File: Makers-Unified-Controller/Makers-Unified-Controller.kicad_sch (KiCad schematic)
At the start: 52 parts

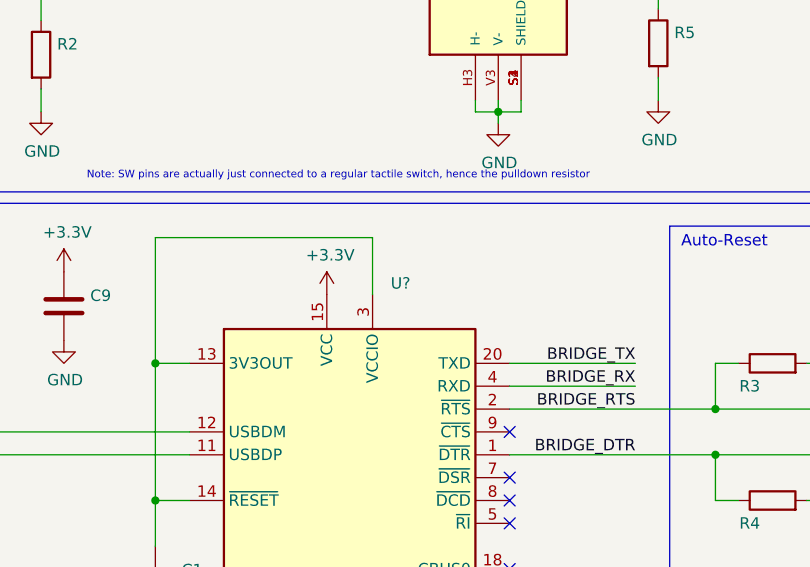
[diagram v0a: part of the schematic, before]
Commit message: Started PCB - removed unused components from revision 1
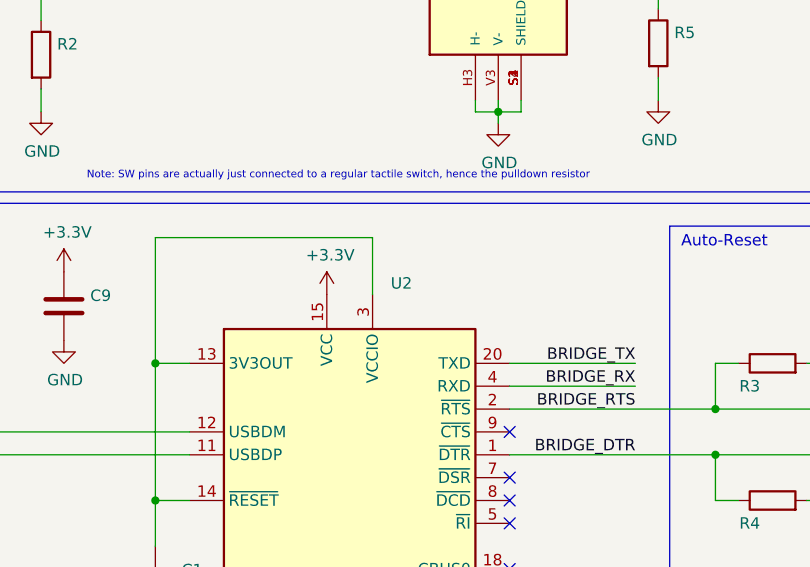
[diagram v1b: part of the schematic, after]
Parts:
- gave numbers to parts that had none: 1

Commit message: fixed BOM item in schematic
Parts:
- U2: digikey_part_number 768-1129-2-ND -> 768-1129-1-ND
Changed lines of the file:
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@@
       (effects (font (size 1.27 1.27)) hide)
     )
-    (property "digikey_part_number" "768-1129-2-ND" (id 4) (at 88.9 144.78 0)
+    (property "digikey_part_number" "768-1129-1-ND" (id 4) (at 88.9 144.78 0)
       (effects (font (size 1.27 1.27)) hide)
     )
@@
     )
     (path "/63021d15-d11b-49d2-bf84-ec09f8b47294/c1425608-5e6d-47c6-a403-895cf960b962"
-      (reference "BT1") (unit 1) (value "PRT-18286") (footprint "Footprint_Imports:PRT18286")
+      (reference "BT1") (unit 1) (value "PRT-18286") (footprint "")
     )
     (path "/00000000-0000-0000-0000-000061acf723"
@@
     )
     (path "/63021d15-d11b-49d2-bf84-ec09f8b47294/048c9335-6615-4fe1-b210-c5621bed4995"
-      (reference "C2") (unit 1) (value "10u") (footprint "Capacitor_SMD:C_0805_2012Metric_Pad1.18x1.45mm_HandSolder")
+      (reference "C2") (unit 1) (value "10u") (footprint "")
     )
     (path "/63021d15-d11b-49d2-bf84-ec09f8b47294/a84c97dc-224b-4aee-818b-6b0092e5b819"
-      (reference "C3") (unit 1) (value "10u") (footprint "Capacitor_SMD:C_0805_2012Metric_Pad1.18x1.45mm_HandSolder")
+      (reference "C3") (unit 1) (value "10u") (footprint "")
     )
     (path "/63021d15-d11b-49d2-bf84-ec09f8b47294/757e3b26-2b31-49bc-b43c-2c2f829aa0f5"
-      (reference "C4") (unit 1) (value "1u") (footprint "Capacitor_SMD:C_0805_2012Metric_Pad1.18x1.45mm_HandSolder")
+      (reference "C4") (unit 1) (value "1u") (footprint "")
     )
     (path "/63021d15-d11b-49d2-bf84-ec09f8b47294/773ea289-2ea8-4dad-a616-30a00b2685df"
-      (reference "C5") (unit 1) (value "10u") (footprint "Capacitor_SMD:C_0805_2012Metric_Pad1.18x1.45mm_HandSolder")
+      (reference "C5") (unit 1) (value "10u") (footprint "")
     )
     (path "/00000000-0000-0000-0000-000061c00f7e"
@@
     )
     (path "/63021d15-d11b-49d2-bf84-ec09f8b47294/47e5ef08-fa75-4d24-9aee-8b0ffa6fb6f8"
-      (reference "C12") (unit 1) (value "10u") (footprint "Capacitor_SMD:C_0805_2012Metric_Pad1.18x1.45mm_HandSolder")
+      (reference "C12") (unit 1) (value "10u") (footprint "")
     )
     (path "/63021d15-d11b-49d2-bf84-ec09f8b47294/82d44cbf-46d2-4460-92df-be60adba77ac"
-      (reference "C13") (unit 1) (value "1u") (footprint "Capacitor_SMD:C_0805_2012Metric_Pad1.18x1.45mm_HandSolder")
+      (reference "C13") (unit 1) (value "1u") (footprint "")
     )
     (path "/63021d15-d11b-49d2-bf84-ec09f8b47294/22906075-5232-413a-b1ac-5482d7041b70"
-      (reference "D1") (unit 1) (value "CDBA340-G") (footprint "Diode_SMD:D_SMA")
+      (reference "D1") (unit 1) (value "CDBA340-G") (footprint "")
     )
     (path "/00000000-0000-0000-0000-000062e0c87c"
@@
     )
     (path "/63021d15-d11b-49d2-bf84-ec09f8b47294/9ada8e2b-05de-4ccd-9d6a-3c1451c5a7f6"
-      (reference "J3") (unit 1) (value "BAT Connector") (footprint "Footprint_Imports:PRT-18286 Connector")
+      (reference "J3") (unit 1) (value "BAT Connector") (footprint "")
     )
     (path "/63021d15-d11b-49d2-bf84-ec09f8b47294/f9f63ee3-19d9-4b43-a1dd-d33705ab9e86"
-      (reference "L1") (unit 1) (value "6.2u") (footprint "Inductor_SMD:L_6.3x6.3_H3")
+      (reference "L1") (unit 1) (value "6.2u") (footprint "")
     )
     (path "/63021d15-d11b-49d2-bf84-ec09f8b47294/cb9803fd-9c70-4aa2-9fdd-1d430b4c3f7b"
-      (reference "Q1") (unit 1) (value "PJA3401A_R1_00001") (footprint "Package_TO_SOT_SMD:SOT-23")
+      (reference "Q1") (unit 1) (value "PJA3401A_R1_00001") (footprint "")
     )
     (path "/00000000-0000-0000-0000-000061b1a432"
@@
     )
     (path "/63021d15-d11b-49d2-bf84-ec09f8b47294/c15d8e35-a568-4071-9637-a6bd86e8dd86"
-      (reference "R1") (unit 1) (value "2.2k") (footprint "Resistor_SMD:R_0805_2012Metric_Pad1.20x1.40mm_HandSolder")
+      (reference "R1") (unit 1) (value "2.2k") (footprint "")
     )
     (path "/00000000-0000-0000-0000-000061c7c689"
@@
     )
     (path "/63021d15-d11b-49d2-bf84-ec09f8b47294/33bac71a-b9a7-48ec-985e-17f75b3744b0"
-      (reference "R6") (unit 1) (value "10k") (footprint "Resistor_SMD:R_0805_2012Metric_Pad1.20x1.40mm_HandSolder")
+      (reference "R6") (unit 1) (value "10k") (footprint "")
     )
     (path "/00000000-0000-0000-0000-000061b94bcc"
@@
     )
     (path "/63021d15-d11b-49d2-bf84-ec09f8b47294/f3156145-19ea-4752-ad0b-81458c22b10b"
-      (reference "SW1") (unit 1) (value "SW_DPDT_x2") (footprint "Footprint_Imports:SW_L102021ML04Q")
+      (reference "SW1") (unit 1) (value "SW_DPDT_x2") (footprint "")
     )
     (path "/00000000-0000-0000-0000-000061b7045a"
@@
     )
     (path "/63021d15-d11b-49d2-bf84-ec09f8b47294/9acf6230-1cca-4a26-aea4-4b4f74711069"
-      (reference "U3") (unit 1) (value "MCP73832-2-OT") (footprint "Package_TO_SOT_SMD:SOT-23-5")
+      (reference "U3") (unit 1) (value "MCP73832-2-OT") (footprint "")
     )
     (path "/00000000-0000-0000-0000-000061ca1f4b"
@@
     )
     (path "/63021d15-d11b-49d2-bf84-ec09f8b47294/faae9d2c-d2ec-4876-a54c-b7f99c6f960b"
-      (reference "U6") (unit 1) (value "TPS62046DRCR") (footprint "Package_SON:VSON-10-1EP_3x3mm_P0.5mm_EP1.2x2mm_ThermalVias")
+      (reference "U6") (unit 1) (value "TPS62046DRCR") (footprint "")
     )
   )

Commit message: Finalized layout and exported files
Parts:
- Q2, Q3: footprint (none) -> Package_TO_SOT_SMD:SOT-23
- SW10, SW11, SW12, SW13, SW2, SW3, SW6, SW7, SW8, SW9: footprint (none) -> Footprint_Imports:SW_1571563-4
- U1, U4: footprint (none) -> XDCR_COM-09032; digikey_part_number 1568-1526-ND -> COM-09032
- U2: footprint (none) -> Package_SO:SSOP-20_3.9x8.7mm_P0.635mm
- U5: footprint (none) -> RF_Module:ESP32-WROOM-32
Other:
- note added: "Note: The ESP32 requires a special reset condition in order to enter programming mode, this is accomplished through the RTS and DTR pins of the FT231XS along with the added transistors. In the event that the controller isn't programming hold the IO0 button then press the EN button, continue holding IO0 until programming is complete"
- note added: "Power Management"
- note removed: "Note: The ESP32 requires a special reset condition in order to enter programming mode, this is accomplished through the RTS and DTR pins of the FT231XQ along with the added transistors. In the event that the controller isn't programming hold the IO0 button then press the EN button, continue holding IO0 until programming is complete"

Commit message: minor edits
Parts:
- Q2, Q3: footprint Package_TO_SOT_SMD:SOT-23 -> (none)
- SW10, SW11, SW12, SW13, SW2, SW3, SW6, SW7, SW8, SW9: footprint Footprint_Imports:SW_1571563-4 -> (none)
- U1, U4: footprint XDCR_COM-09032 -> (none)
- U2: footprint Package_SO:SSOP-20_3.9x8.7mm_P0.635mm -> (none)
- U5: footprint RF_Module:ESP32-WROOM-32 -> (none)
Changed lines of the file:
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@@
       (effects (font (size 1.27 1.27)) (justify left))
     )
-    (property "Footprint" "Package_TO_SOT_SMD:SOT-23" (id 2) (at 151.13 131.445 0)
+    (property "Footprint" "" (id 2) (at 151.13 131.445 0)
       (effects (font (size 1.27 1.27) italic) (justify left) hide)
     )
@@
       (effects (font (size 1.27 1.27)) (justify left))
     )
-    (property "Footprint" "Package_TO_SOT_SMD:SOT-23" (id 2) (at 151.13 142.875 0)
+    (property "Footprint" "" (id 2) (at 151.13 142.875 0)
       (effects (font (size 1.27 1.27) italic) (justify left) hide)
     )
@@
     (property "Reference" "SW3" (id 0) (at 129.54 175.641 0))
     (property "Value" "" (id 1) (at 129.54 177.9524 0))
-    (property "Footprint" "Footprint_Imports:SW_1571563-4" (id 2) (at 129.54 177.8 0)
+    (property "Footprint" "" (id 2) (at 129.54 177.8 0)
       (effects (font (size 1.27 1.27)) hide)
     )
@@
     (property "Reference" "SW2" (id 0) (at 129.54 164.211 0))
     (property "Value" "" (id 1) (at 129.54 166.5224 0))
-    (property "Footprint" "Footprint_Imports:SW_1571563-4" (id 2) (at 129.54 166.37 0)
+    (property "Footprint" "" (id 2) (at 129.54 166.37 0)
       (effects (font (size 1.27 1.27)) hide)
     )
@@
       (effects (font (size 1.27 1.27)) (justify left))
     )
-    (property "Footprint" "XDCR_COM-09032" (id 2) (at 36.83 85.09 0)
+    (property "Footprint" "" (id 2) (at 36.83 85.09 0)
       (effects (font (size 1.27 1.27)) (justify left bottom) hide)
     )
@@
       (effects (font (size 1.27 1.27)) (justify left))
     )
-    (property "Footprint" "XDCR_COM-09032" (id 2) (at 105.41 83.82 0)
+    (property "Footprint" "" (id 2) (at 105.41 83.82 0)
       (effects (font (size 1.27 1.27)) (justify left bottom) hide)
     )
@@
       (effects (font (size 1.27 1.27)) (justify left))
     )
-    (property "Footprint" "Footprint_Imports:SW_1571563-4" (id 2) (at 210.82 30.48 0)
+    (property "Footprint" "" (id 2) (at 210.82 30.48 0)
       (effects (font (size 1.27 1.27)) hide)
     )
@@
     (property "Reference" "U5" (id 0) (at 220.98 62.23 0))
     (property "Value" "" (id 1) (at 229.235 64.77 0))
-    (property "Footprint" "RF_Module:ESP32-WROOM-32" (id 2) (at 214.63 138.43 0)
+    (property "Footprint" "" (id 2) (at 214.63 138.43 0)
       (effects (font (size 1.27 1.27)) hide)
     )
@@
       (effects (font (size 1.27 1.27)) (justify left))
     )
-    (property "Footprint" "Footprint_Imports:SW_1571563-4" (id 2) (at 223.52 30.48 0)
+    (property "Footprint" "" (id 2) (at 223.52 30.48 0)
       (effects (font (size 1.27 1.27)) hide)
     )
@@
       (effects (font (size 1.27 1.27)) (justify left))
     )
-    (property "Footprint" "Footprint_Imports:SW_1571563-4" (id 2) (at 237.49 30.48 0)
+    (property "Footprint" "" (id 2) (at 237.49 30.48 0)
       (effects (font (size 1.27 1.27)) hide)
     )
@@
       (effects (font (size 1.27 1.27)) (justify left))
     )
-    (property "Footprint" "Footprint_Imports:SW_1571563-4" (id 2) (at 250.19 30.48 0)
+    (property "Footprint" "" (id 2) (at 250.19 30.48 0)
       (effects (font (size 1.27 1.27)) hide)
     )
@@
       (effects (font (size 1.27 1.27)) (justify left))
     )
-    (property "Footprint" "Footprint_Imports:SW_1571563-4" (id 2) (at 262.89 30.48 0)
+    (property "Footprint" "" (id 2) (at 262.89 30.48 0)
       (effects (font (size 1.27 1.27)) hide)
     )
@@
       (effects (font (size 1.27 1.27)) (justify left))
     )
-    (property "Footprint" "Footprint_Imports:SW_1571563-4" (id 2) (at 275.59 30.48 0)
+    (property "Footprint" "" (id 2) (at 275.59 30.48 0)
       (effects (font (size 1.27 1.27)) hide)
     )
@@
       (effects (font (size 1.27 1.27)) (justify left))
     )
-    (property "Footprint" "Footprint_Imports:SW_1571563-4" (id 2) (at 196.85 30.48 0)
+    (property "Footprint" "" (id 2) (at 196.85 30.48 0)
       (effects (font (size 1.27 1.27)) hide)
     )
@@
       (effects (font (size 1.27 1.27)) (justify left))
     )
-    (property "Footprint" "Footprint_Imports:SW_1571563-4" (id 2) (at 182.88 30.48 0)
+    (property "Footprint" "" (id 2) (at 182.88 30.48 0)
       (effects (font (size 1.27 1.27)) hide)
     )
@@
       (effects (font (size 1.27 1.27)) (justify left))
     )
-    (property "Footprint" "Package_SO:SSOP-20_3.9x8.7mm_P0.635mm" (id 2) (at 114.3 165.1 0)
+    (property "Footprint" "" (id 2) (at 114.3 165.1 0)
       (effects (font (size 1.27 1.27)) hide)
     )
@@
     )
     (path "/63021d15-d11b-49d2-bf84-ec09f8b47294/048c9335-6615-4fe1-b210-c5621bed4995"
-      (reference "C2") (unit 1) (value "10u") (footprint "Capacitor_SMD:C_0805_2012Metric_Pad1.18x1.45mm_HandSolder")
+      (reference "C2") (unit 1) (value "10u") (footprint "")
     )
     (path "/63021d15-d11b-49d2-bf84-ec09f8b47294/a84c97dc-224b-4aee-818b-6b0092e5b819"
-      (reference "C3") (unit 1) (value "10u") (footprint "Capacitor_SMD:C_0805_2012Metric_Pad1.18x1.45mm_HandSolder")
+      (reference "C3") (unit 1) (value "10u") (footprint "")
     )
     (path "/63021d15-d11b-49d2-bf84-ec09f8b47294/757e3b26-2b31-49bc-b43c-2c2f829aa0f5"
-      (reference "C4") (unit 1) (value "1u") (footprint "Capacitor_SMD:C_0805_2012Metric_Pad1.18x1.45mm_HandSolder")
+      (reference "C4") (unit 1) (value "1u") (footprint "")
     )
     (path "/63021d15-d11b-49d2-bf84-ec09f8b47294/773ea289-2ea8-4dad-a616-30a00b2685df"
-      (reference "C5") (unit 1) (value "10u") (footprint "Capacitor_SMD:C_0805_2012Metric_Pad1.18x1.45mm_HandSolder")
+      (reference "C5") (unit 1) (value "10u") (footprint "")
     )
     (path "/00000000-0000-0000-0000-000061c00f7e"
@@
     )
     (path "/63021d15-d11b-49d2-bf84-ec09f8b47294/47e5ef08-fa75-4d24-9aee-8b0ffa6fb6f8"
-      (reference "C12") (unit 1) (value "10u") (footprint "Capacitor_SMD:C_0805_2012Metric_Pad1.18x1.45mm_HandSolder")
+      (reference "C12") (unit 1) (value "10u") (footprint "")
     )
     (path "/63021d15-d11b-49d2-bf84-ec09f8b47294/82d44cbf-46d2-4460-92df-be60adba77ac"
-      (reference "C13") (unit 1) (value "1u") (footprint "Capacitor_SMD:C_0805_2012Metric_Pad1.18x1.45mm_HandSolder")
+      (reference "C13") (unit 1) (value "1u") (footprint "")
     )
     (path "/63021d15-d11b-49d2-bf84-ec09f8b47294/22906075-5232-413a-b1ac-5482d7041b70"
-      (reference "D1") (unit 1) (value "CDBA340-G") (footprint "Diode_SMD:D_SMA")
+      (reference "D1") (unit 1) (value "CDBA340-G") (footprint "")
     )
     (path "/00000000-0000-0000-0000-000062e0c87c"
@@
     )
     (path "/63021d15-d11b-49d2-bf84-ec09f8b47294/9ada8e2b-05de-4ccd-9d6a-3c1451c5a7f6"
-      (reference "J3") (unit 1) (value "BAT Connector") (footprint "Footprint_Imports:PRT-18286 Connector")
+      (reference "J3") (unit 1) (value "BAT Connector") (footprint "")
     )
     (path "/63021d15-d11b-49d2-bf84-ec09f8b47294/f9f63ee3-19d9-4b43-a1dd-d33705ab9e86"
-      (reference "L1") (unit 1) (value "6.2u") (footprint "Inductor_SMD:L_6.3x6.3_H3")
+      (reference "L1") (unit 1) (value "6.2u") (footprint "")
     )
     (path "/63021d15-d11b-49d2-bf84-ec09f8b47294/cb9803fd-9c70-4aa2-9fdd-1d430b4c3f7b"
@@
     )
     (path "/63021d15-d11b-49d2-bf84-ec09f8b47294/c15d8e35-a568-4071-9637-a6bd86e8dd86"
-      (reference "R1") (unit 1) (value "2.2k") (footprint "Resistor_SMD:R_0805_2012Metric_Pad1.20x1.40mm_HandSolder")
+      (reference "R1") (unit 1) (value "2.2k") (footprint "")
     )
     (path "/00000000-0000-0000-0000-000061c7c689"
@@
     )
     (path "/63021d15-d11b-49d2-bf84-ec09f8b47294/33bac71a-b9a7-48ec-985e-17f75b3744b0"
-      (reference "R6") (unit 1) (value "10k") (footprint "Resistor_SMD:R_0805_2012Metric_Pad1.20x1.40mm_HandSolder")
+      (reference "R6") (unit 1) (value "10k") (footprint "")
     )
     (path "/00000000-0000-0000-0000-000061b94bcc"
@@
     )
     (path "/63021d15-d11b-49d2-bf84-ec09f8b47294/f3156145-19ea-4752-ad0b-81458c22b10b"
-      (reference "SW1") (unit 1) (value "SW_DPDT_x2") (footprint "Footprint_Imports:SW_L102021ML04Q")
+      (reference "SW1") (unit 1) (value "SW_DPDT_x2") (footprint "")
     )
     (path "/00000000-0000-0000-0000-000061b7045a"
@@
     )
     (path "/63021d15-d11b-49d2-bf84-ec09f8b47294/9acf6230-1cca-4a26-aea4-4b4f74711069"
-      (reference "U3") (unit 1) (value "MCP73832-2-OT") (footprint "Package_TO_SOT_SMD:SOT-23-5")
+      (reference "U3") (unit 1) (value "MCP73832-2-0T") (footprint "Package_TO_SOT_SMD:SOT-23-5")
     )
     (path "/00000000-0000-0000-0000-000061ca1f4b"

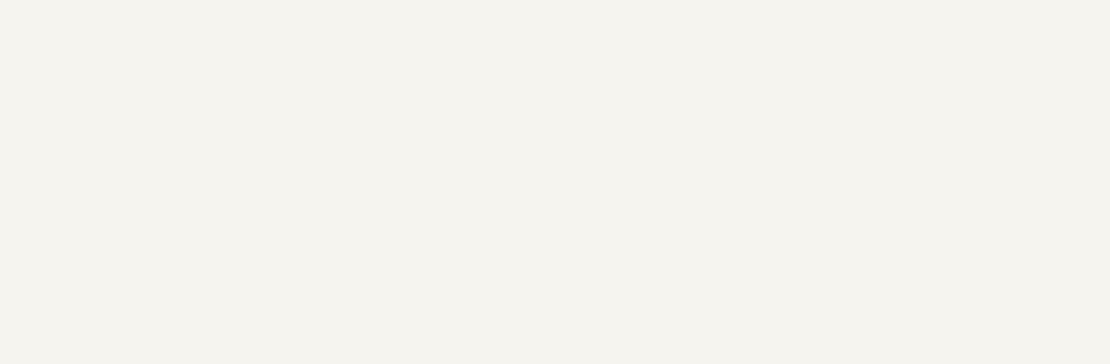
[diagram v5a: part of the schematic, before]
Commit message: minor edits to schematic and Ibom
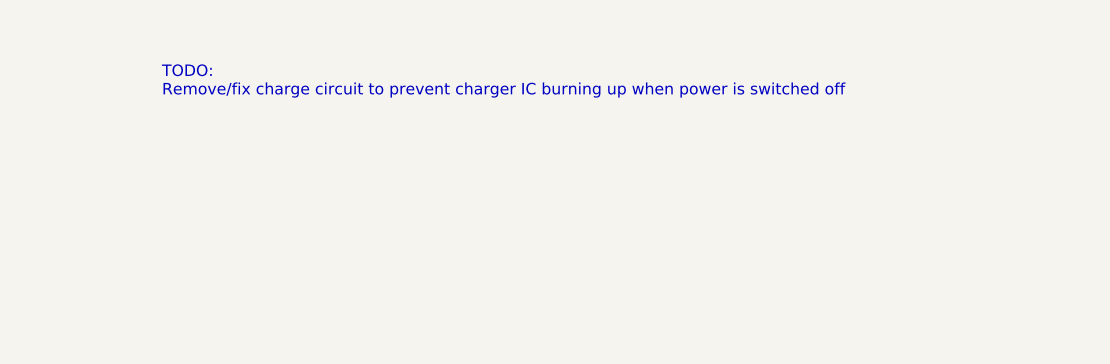
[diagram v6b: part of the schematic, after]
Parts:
- R19, R21: LCSC_part_number C17710 -> (none); digikey_part_number P16048CT-ND -> RMCF0805JT2K20CT-ND
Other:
- note added: "TODO: Remove/fix charge circuit to prevent charger IC burning up when power is switched off"
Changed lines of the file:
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@@
+    (effects (font (size 1.27 1.27)) (justify left bottom))
+  )
+  (text "TODO: \nRemove/fix charge circuit to prevent charger IC burning up when power is switched off"
+    (at 303.53 22.86 0)
     (effects (font (size 1.27 1.27)) (justify left bottom))
   )
@@
       (effects (font (size 1.27 1.27)) hide)
     )
-    (property "digikey_part_number" "P16048CT-ND" (id 4) (at 259.08 120.65 0)
-      (effects (font (size 1.27 1.27)) hide)
-    )
-    (property "LCSC_part_number" "C17710" (id 5) (at 259.08 120.65 0)
+    (property "digikey_part_number" "RMCF0805JT2K20CT-ND" (id 4) (at 259.08 120.65 0)
+      (effects (font (size 1.27 1.27)) hide)
+    )
+    (property "LCSC_part_number" "" (id 5) (at 259.08 120.65 0)
       (effects (font (size 1.27 1.27)) hide)
     )
@@
       (effects (font (size 1.27 1.27)) hide)
     )
-    (property "digikey_part_number" "P16048CT-ND" (id 4) (at 271.78 114.3 0)
-      (effects (font (size 1.27 1.27)) hide)
-    )
-    (property "LCSC_part_number" "C17710" (id 5) (at 271.78 114.3 0)
+    (property "digikey_part_number" "RMCF0805JT2K20CT-ND" (id 4) (at 271.78 114.3 0)
       (effects (font (size 1.27 1.27)) hide)
     )
@@
     )
     (path "/63021d15-d11b-49d2-bf84-ec09f8b47294/c15d8e35-a568-4071-9637-a6bd86e8dd86"
-      (reference "R1") (unit 1) (value "2.2k") (footprint "")
+      (reference "R1") (unit 1) (value "4.7k") (footprint "")
     )
     (path "/00000000-0000-0000-0000-000061c7c689"
@@
     )
     (path "/00000000-0000-0000-0000-000062e20eb8"
-      (reference "R19") (unit 1) (value "470") (footprint "Resistor_SMD:R_0805_2012Metric_Pad1.20x1.40mm_HandSolder")
+      (reference "R19") (unit 1) (value "2.2k") (footprint "Resistor_SMD:R_0805_2012Metric_Pad1.20x1.40mm_HandSolder")
     )
     (path "/00000000-0000-0000-0000-000061d9e3bc"
@@
     )
     (path "/00000000-0000-0000-0000-000062e21419"
-      (reference "R21") (unit 1) (value "470") (footprint "Resistor_SMD:R_0805_2012Metric_Pad1.20x1.40mm_HandSolder")
+      (reference "R21") (unit 1) (value "2.2k") (footprint "Resistor_SMD:R_0805_2012Metric_Pad1.20x1.40mm_HandSolder")
     )
     (path "/63021d15-d11b-49d2-bf84-ec09f8b47294/f3156145-19ea-4752-ad0b-81458c22b10b"
